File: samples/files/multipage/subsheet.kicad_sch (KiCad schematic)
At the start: 1 part

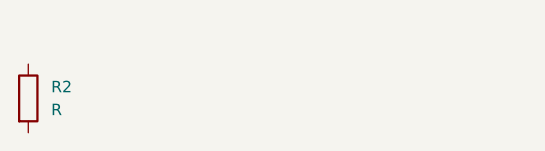
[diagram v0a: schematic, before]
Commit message: implement all schema elements
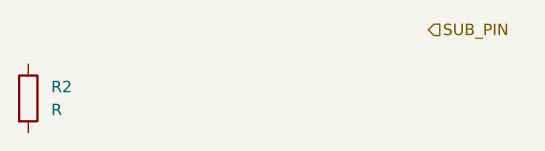
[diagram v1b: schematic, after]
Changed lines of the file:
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@@
 (kicad_sch (version 20211123) (generator eeschema)
   (paper "A4")
+  (hierarchical_label "SUB_PIN" (shape input) (at 157.48 86.36 0)
+    (effects (font (size 1.27 1.27)) (justify left))
+  )
   (symbol (lib_id "Device:R") (at 113.03 93.98 0) (unit 1)
     (in_bom yes) (on_board yes) (fields_autoplaced)
